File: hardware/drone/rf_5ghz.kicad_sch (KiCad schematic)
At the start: 18 parts, among them U7 CC3350, U8 DPX167125DT-8197B1, U9 DEA162450BT-1295A1, Y1 Crystal_GND24

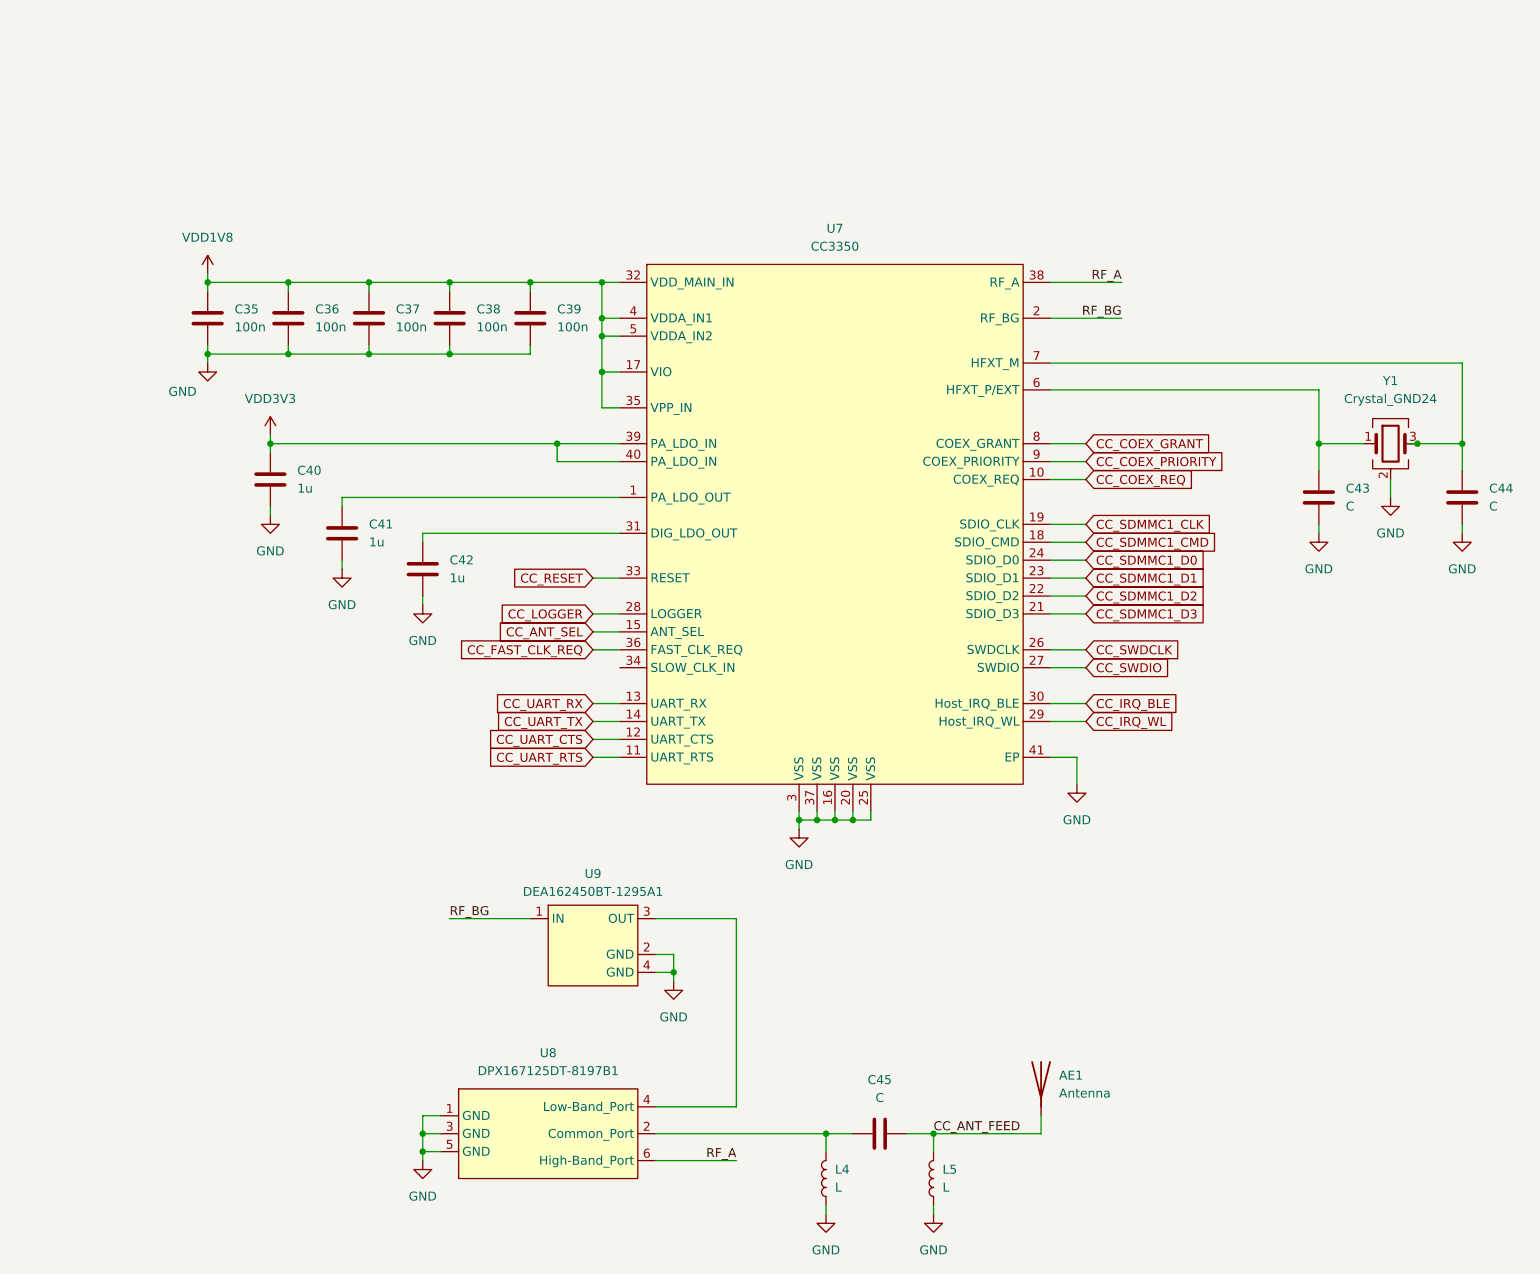
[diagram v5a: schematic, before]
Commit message: Added SWD
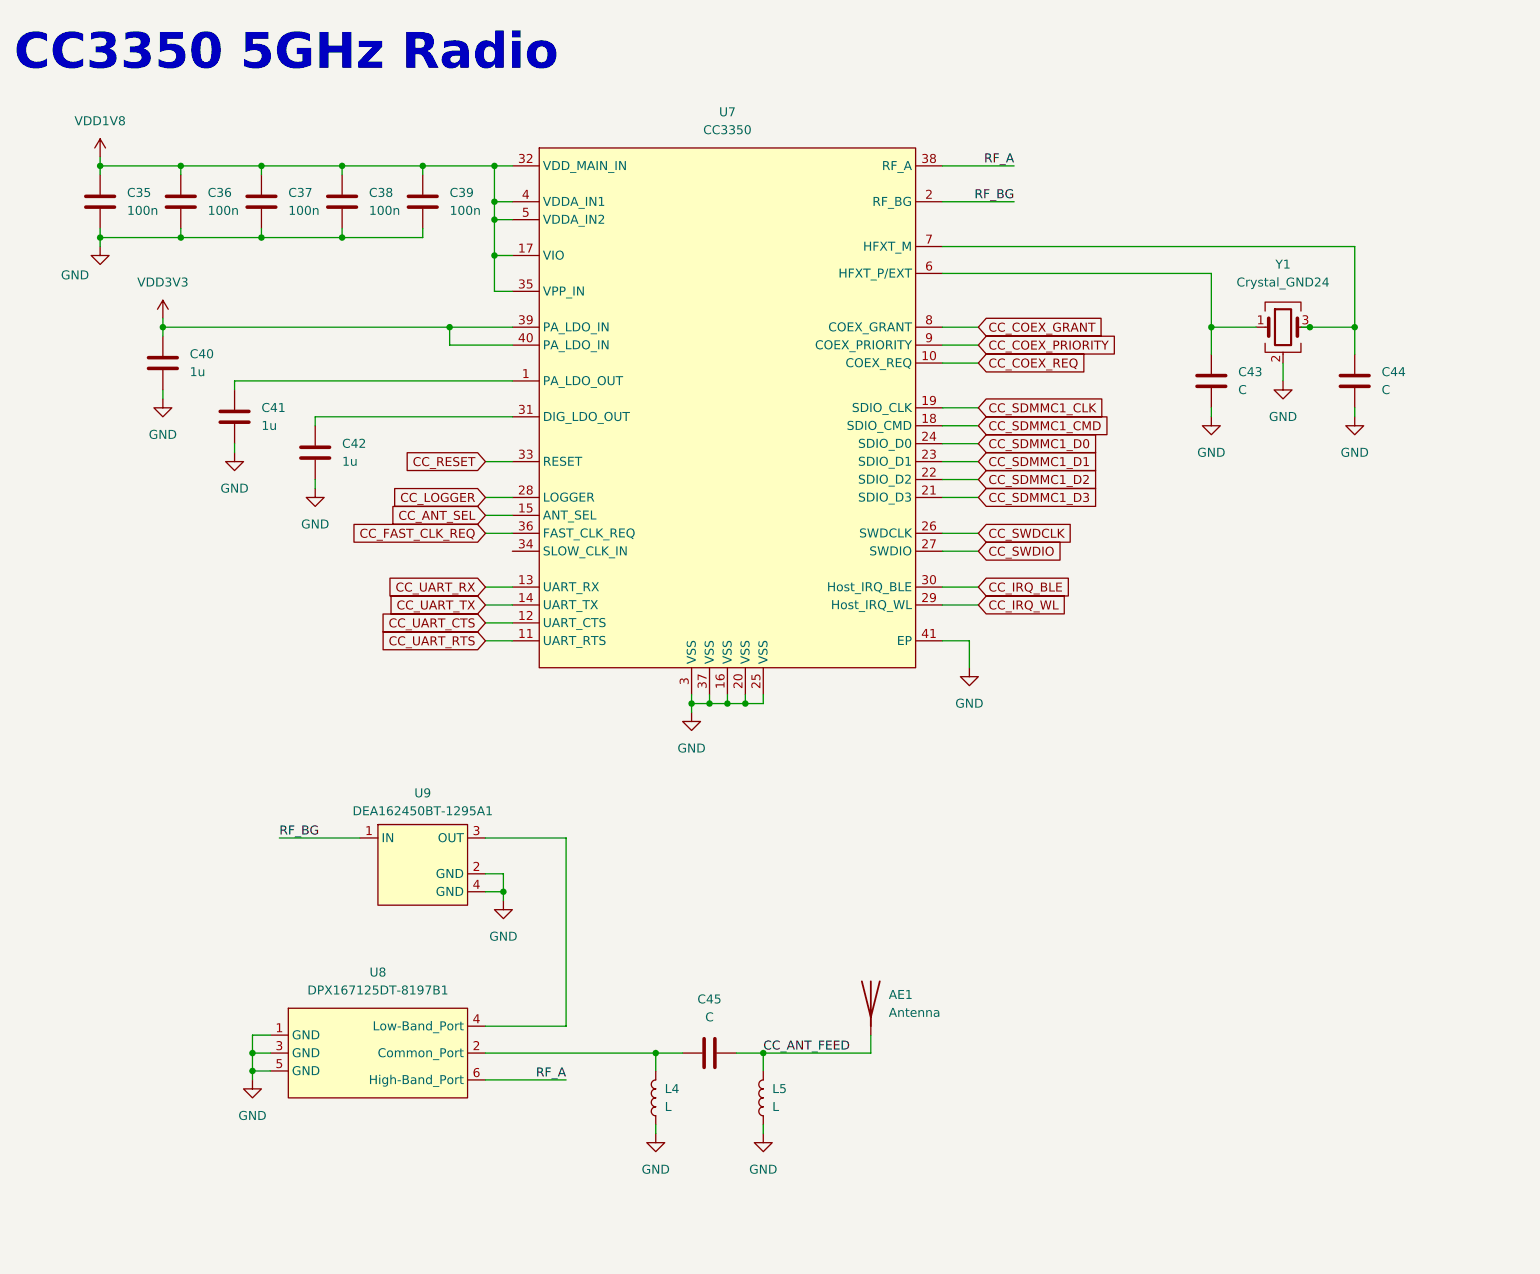
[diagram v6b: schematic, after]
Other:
- note added: "CC3350 5GHz Radio"
- moved on the sheet: AE1, C35, C36, C37, C38, C39, C40, C41, C42, C43, C44, C45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

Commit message: Finished MCU schematic decoupling, finished system control schematic
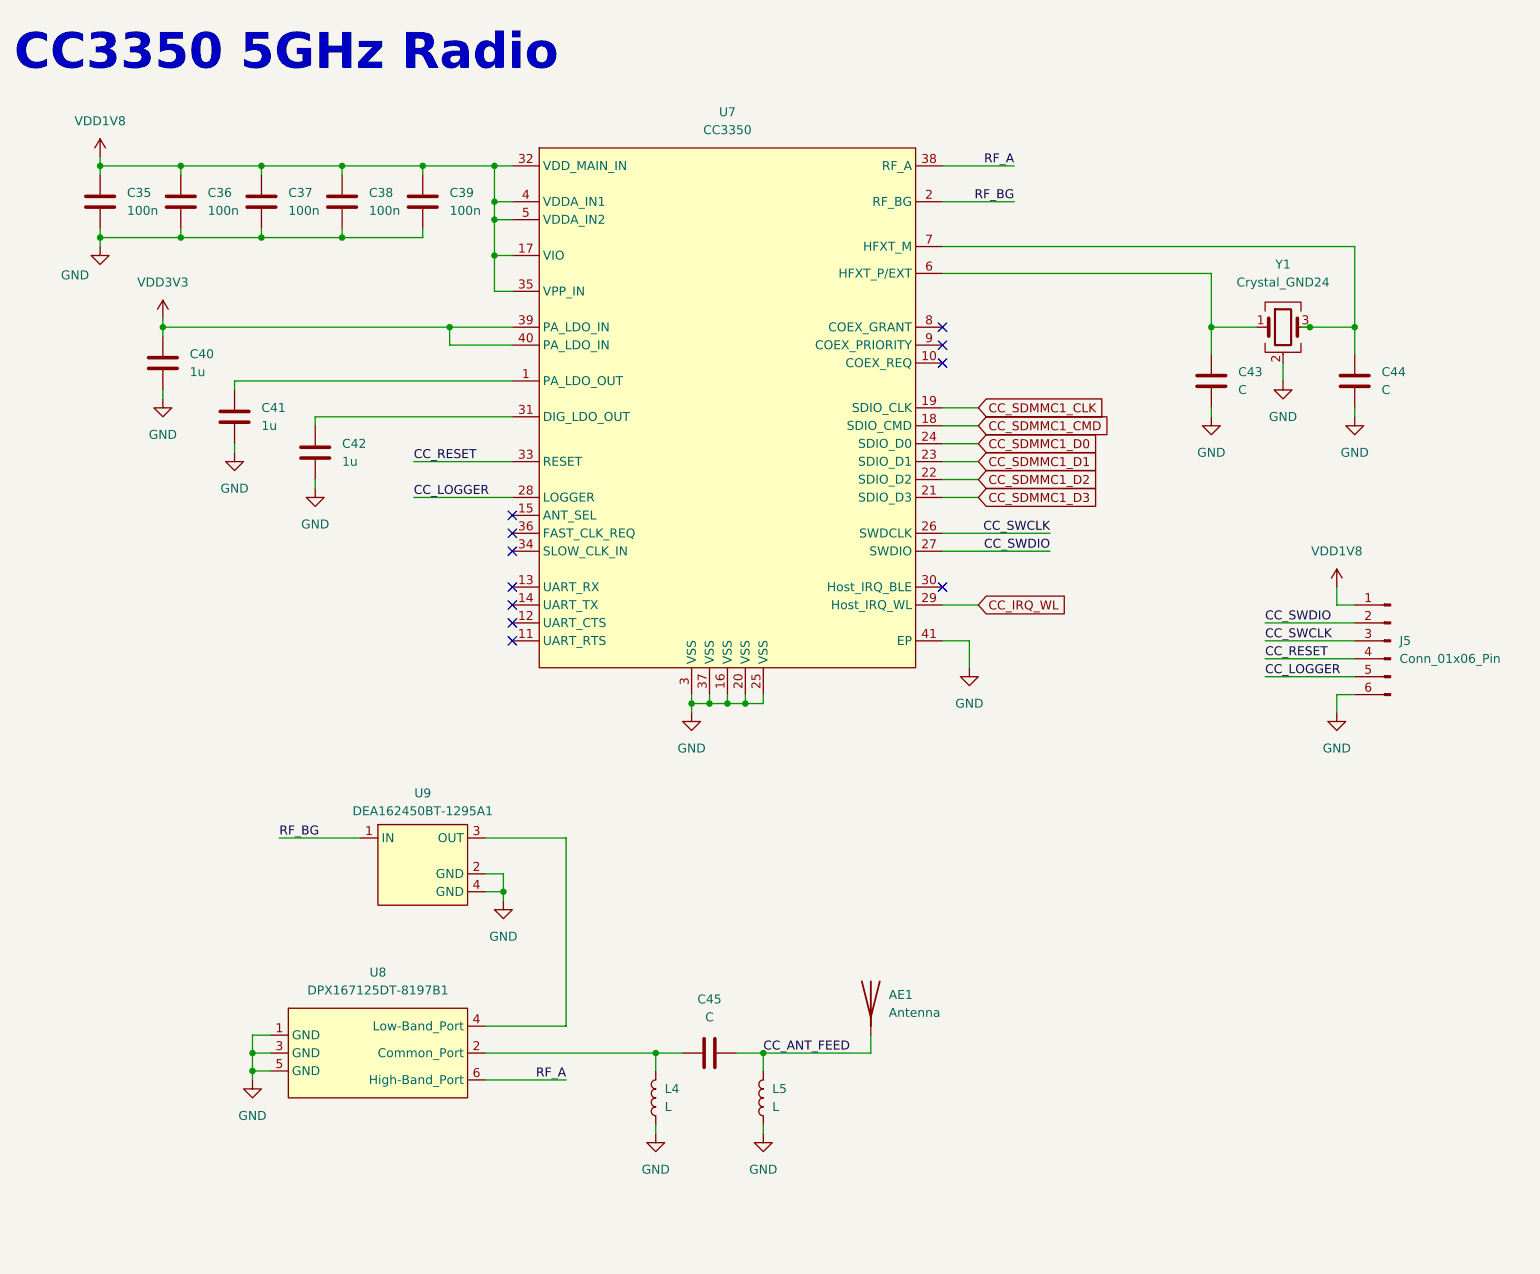
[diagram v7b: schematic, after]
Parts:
- added J5: Conn_01x06_Pin, RF_Module:Ai-Thinker-Ra-01-LoRa, symbol Connector:Conn_01x06_Pin
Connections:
- net CC_LOGGER: now also J5.5 (Pin_5)
- net CC_RESET: now also J5.4 (Pin_4)
- net CC_SWDIO: now also J5.2 (Pin_2)
- net GND: now also J5.6 (Pin_6)
- net VDD1V8: now also J5.1 (Pin_1)
- net CC_ANT_SEL: no longer names the net of U7.15 (ANT_SEL)
- net CC_COEX_GRANT: no longer names the net of U7.8 (COEX_GRANT)
- net CC_COEX_PRIORITY: no longer names the net of U7.9 (COEX_PRIORITY)
- net CC_COEX_REQ: no longer names the net of U7.10 (COEX_REQ)
- net CC_FAST_CLK_REQ: no longer names the net of U7.36 (FAST_CLK_REQ)
- net CC_IRQ_BLE: no longer names the net of U7.30 (Host_IRQ_BLE)
- net CC_SWDCLK renamed CC_SWCLK
- net CC_SWCLK: now also J5.3 (Pin_3)
- net CC_UART_CTS: no longer names the net of U7.12 (UART_CTS)
- net CC_UART_RTS: no longer names the net of U7.11 (UART_RTS)
- net CC_UART_RX: no longer names the net of U7.13 (UART_RX)
- net CC_UART_TX: no longer names the net of U7.14 (UART_TX)
- no-connect marks 0 -> 11

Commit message: Created pinmux table and completed pinmuxing
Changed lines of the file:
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@@
+	(wire
+		(pts
+			(xy 87.63 81.28) (xy 90.17 81.28)
+		)
+		(stroke
+			(width 0)
+			(type default)
+		)
+	)
 	(wire
 		(pts
@@
 	(wire
 		(pts
-			(xy 196.85 109.22) (xy 209.55 109.22)
-		)
-		(stroke
-			(width 0)
-			(type default)
-		)
-	)
-	(wire
-		(pts
 			(xy 118.11 115.57) (xy 118.11 114.3)
 		)
@@
 	(wire
 		(pts
-			(xy 76.2 81.28) (xy 90.17 81.28)
+			(xy 195.58 109.22) (xy 209.55 109.22)
 		)
 		(stroke
@@
 		)
 	)
-	(label "CC_RESET"
-		(at 76.2 81.28 0)
-		(effects
-			(font
-				(size 1.27 1.27)
-			)
-			(justify left bottom)
-		)
-	)
 	(label "CC_SWDIO"
 		(at 196.85 104.14 0)
@@
 	(label "CC_SWCLK"
 		(at 196.85 106.68 0)
-		(effects
-			(font
-				(size 1.27 1.27)
-			)
-			(justify left bottom)
-		)
-	)
-	(label "CC_RESET"
-		(at 196.85 109.22 0)
 		(effects
 			(font
@@
 		)
 	)
+	(global_label "CC_RESET"
+		(shape input)
+		(at 195.58 109.22 180)
+		(fields_autoplaced yes)
+		(effects
+			(font
+				(size 1.27 1.27)
+			)
+			(justify right)
+		)
+		(property "Intersheetrefs" "${INTERSHEET_REFS}"
+			(at 183.3421 109.22 0)
+			(hide yes)
+			(show_name no)
+			(do_not_autoplace no)
+			(effects
+				(font
+					(size 1.27 1.27)
+				)
+				(justify right)
+			)
+		)
+	)
 	(global_label "CC_SDMMC1_D2"
 		(shape input)
@@
 			)
 		)
+	)
+	(global_label "CC_RESET"
+		(shape input)
+		(at 87.63 81.28 180)
+		(fields_autoplaced yes)
+		(effects
+			(font
+				(size 1.27 1.27)
+			)
+			(justify right)
+		)
+		(property "Intersheetrefs" "${INTERSHEET_REFS}"
+			(at 75.3921 81.28 0)
+			(hide yes)
+			(show_name no)
+			(do_not_autoplace no)
+			(effects
+				(font
+					(size 1.27 1.27)
+				)
+				(justify right)
+			)
+		)
